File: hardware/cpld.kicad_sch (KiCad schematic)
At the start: 1 part, among them U26 ATF1508AS-10AU100

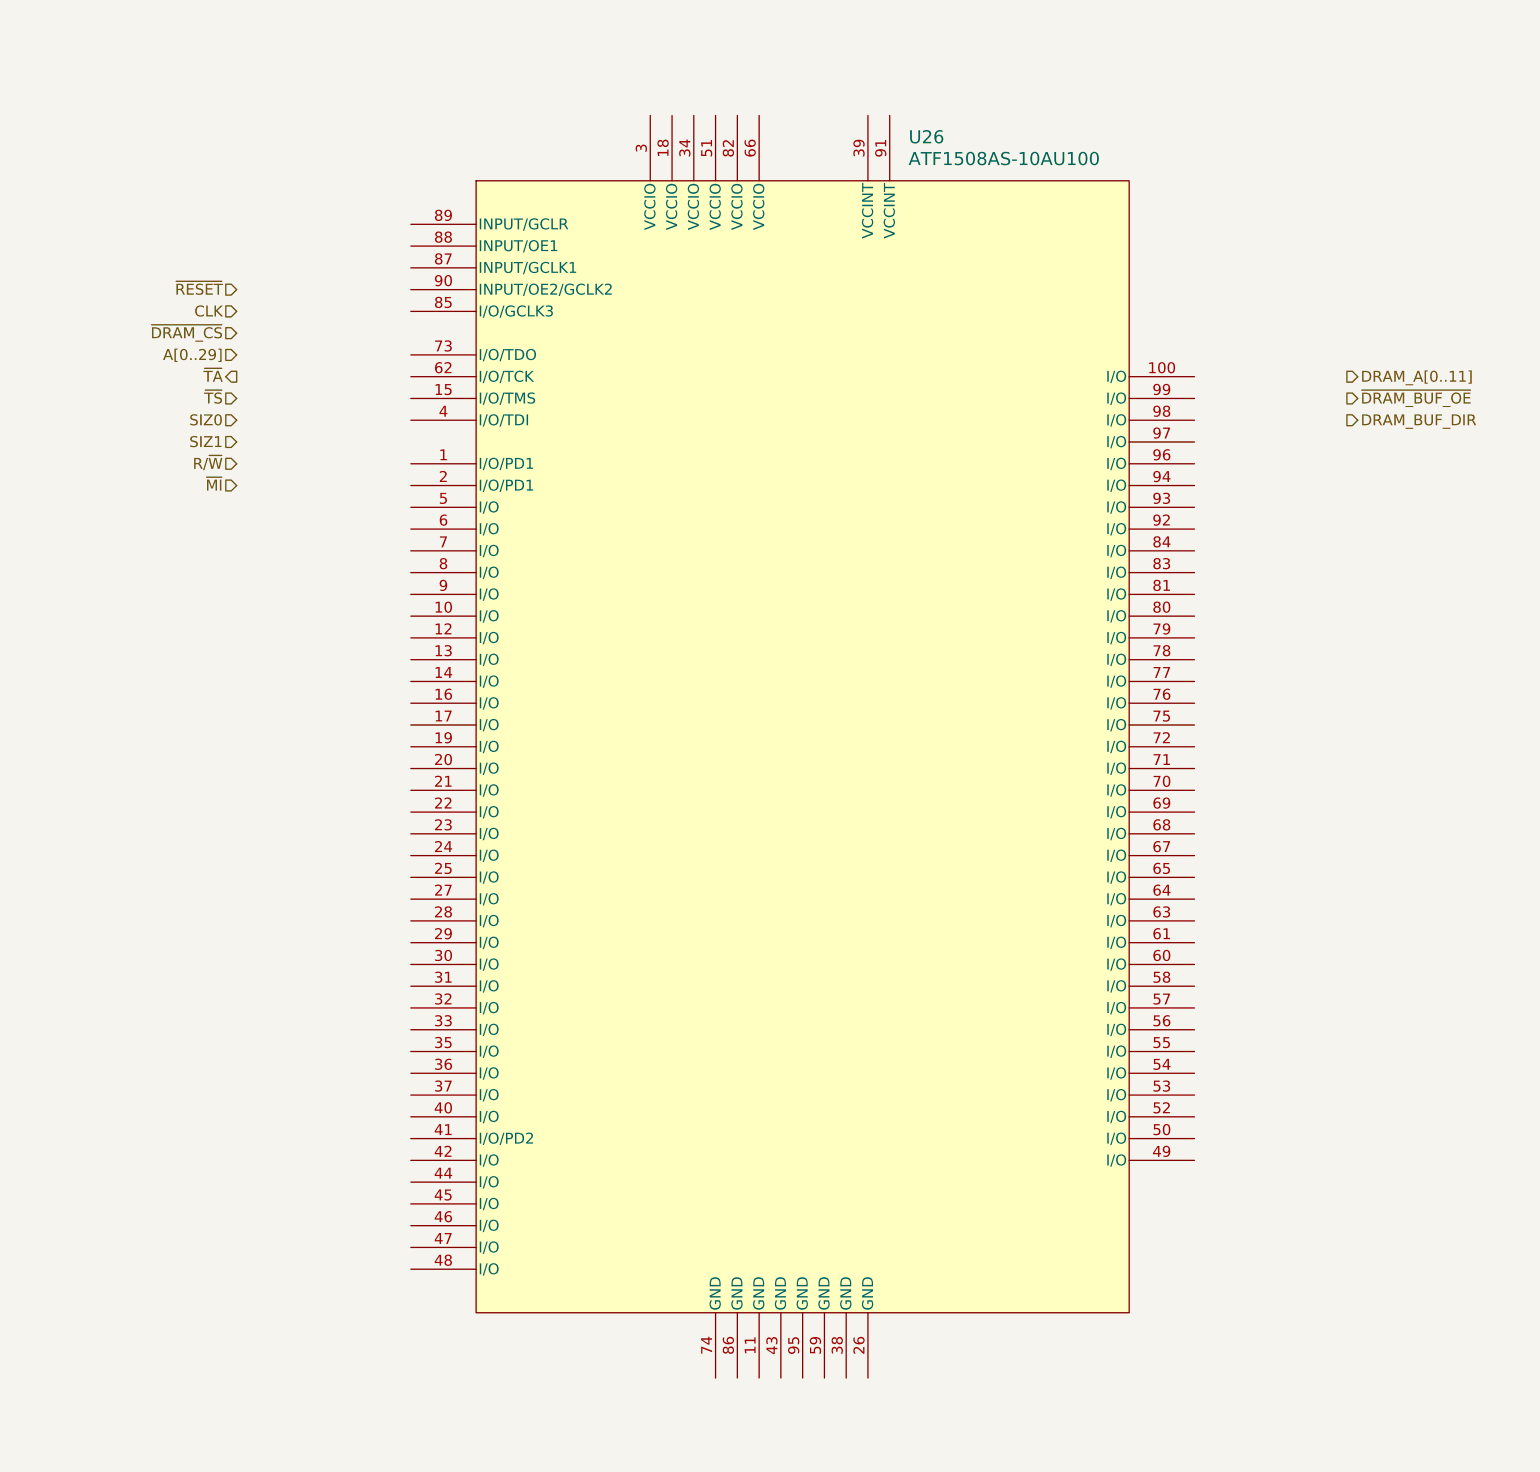
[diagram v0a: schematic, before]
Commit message: add interrupt logic, clean up modules
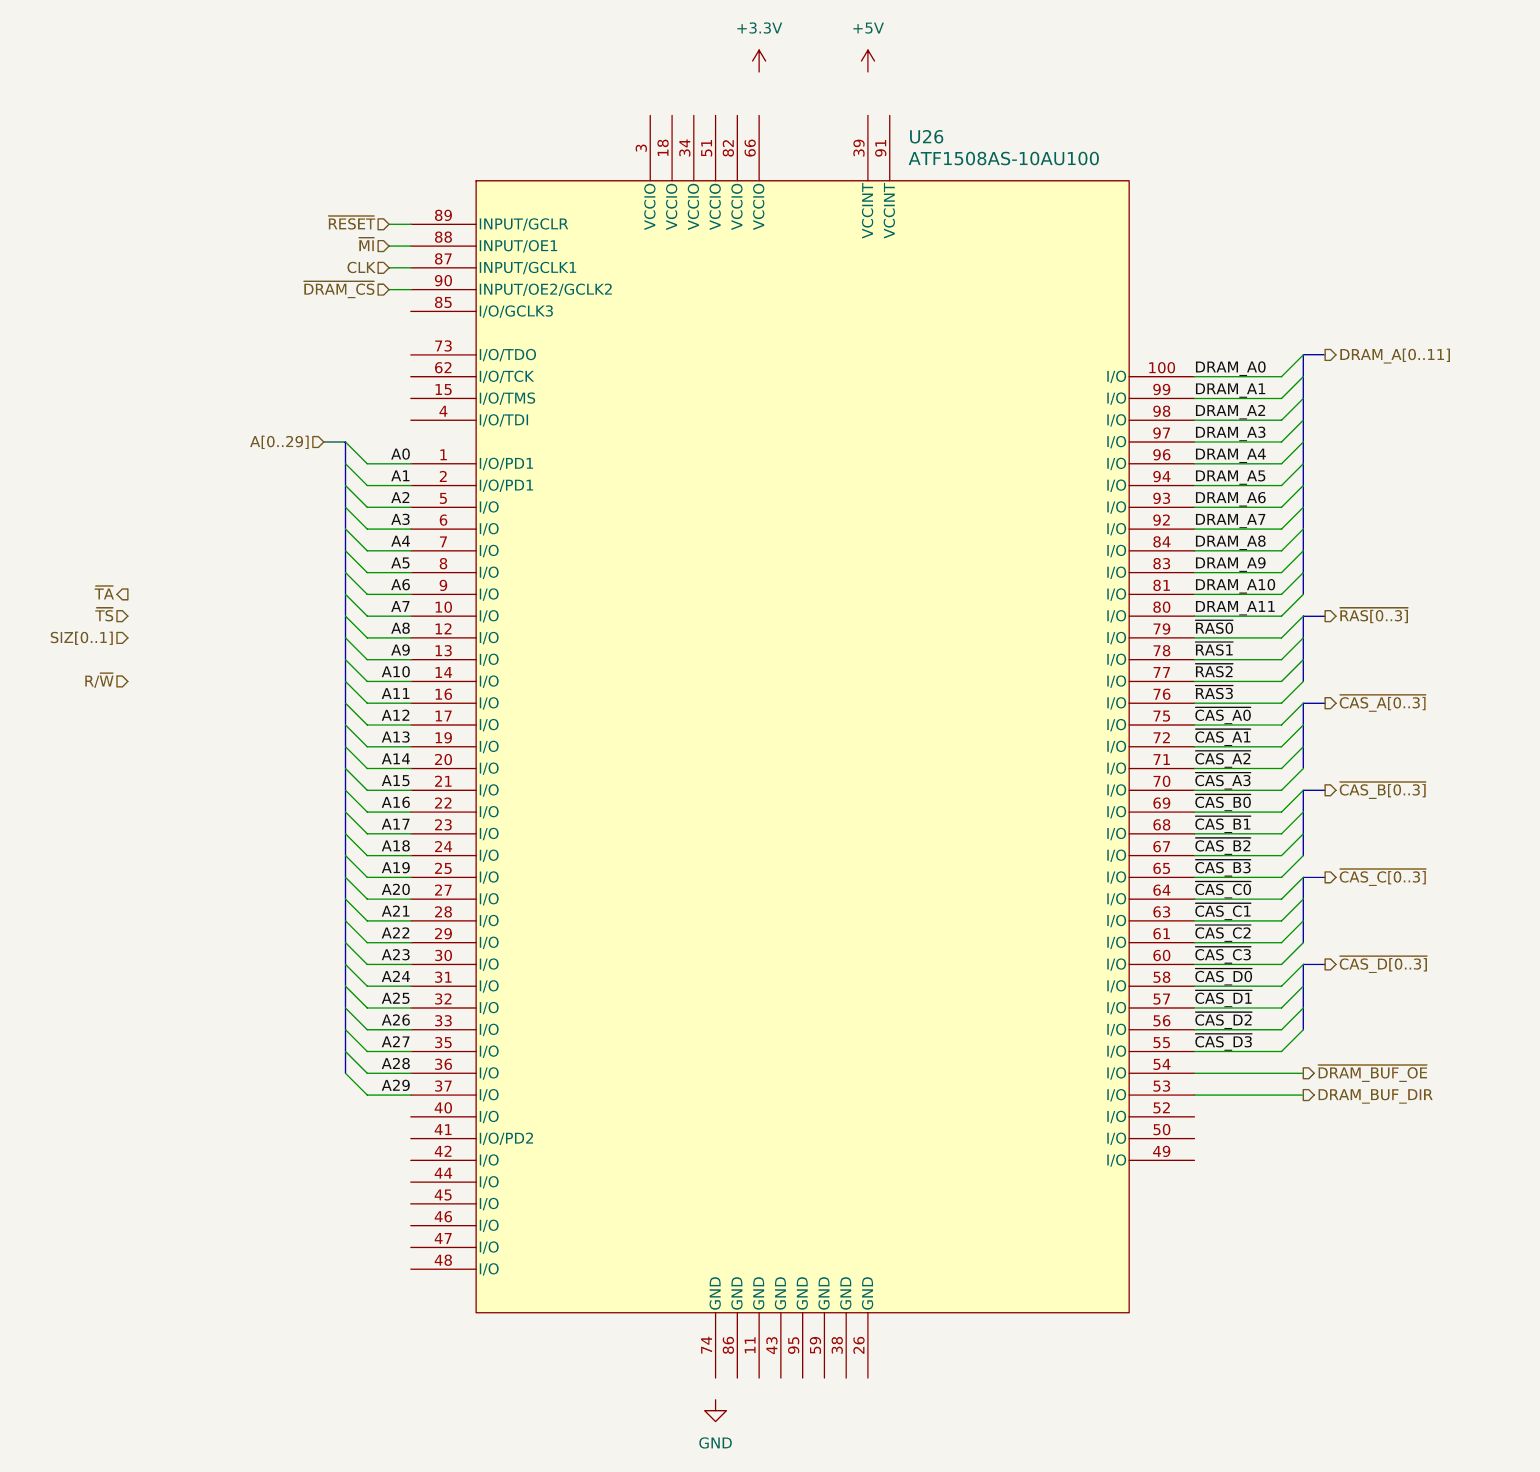
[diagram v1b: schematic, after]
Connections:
- net CLK: now also U26.87 (INPUT/GCLK1)
- net DRAM_BUF_DIR: now also U26.53 (I/O)
- net ~{DRAM_BUF_OE}: now also U26.54 (I/O)
- net ~{DRAM_CS}: now also U26.90 (INPUT/OE2/GCLK2)
- net ~{MI}: now also U26.88 (INPUT/OE1)
- net ~{RESET}: now also U26.89 (INPUT/GCLR)
- net A0: now reaches U26.1 (I/O/PD1)
- net A7: now reaches U26.10 (I/O)
- net DRAM_A0: now reaches U26.100 (I/O)
- net A8: now reaches U26.12 (I/O)
- net A9: now reaches U26.13 (I/O)
- net A10: now reaches U26.14 (I/O)
- net A11: now reaches U26.16 (I/O)
- net A12: now reaches U26.17 (I/O)
- net A13: now reaches U26.19 (I/O)
- net A1: now reaches U26.2 (I/O/PD1)
- net A14: now reaches U26.20 (I/O)
- net A15: now reaches U26.21 (I/O)
- net A16: now reaches U26.22 (I/O)
- net A17: now reaches U26.23 (I/O)
- net A18: now reaches U26.24 (I/O)
- net A19: now reaches U26.25 (I/O)
- net A20: now reaches U26.27 (I/O)
- net A21: now reaches U26.28 (I/O)
- net A22: now reaches U26.29 (I/O)
- net A23: now reaches U26.30 (I/O)
- net A24: now reaches U26.31 (I/O)
- net A25: now reaches U26.32 (I/O)
- net A26: now reaches U26.33 (I/O)
- net A27: now reaches U26.35 (I/O)
- net A28: now reaches U26.36 (I/O)
- net A29: now reaches U26.37 (I/O)
- net A2: now reaches U26.5 (I/O)
- net ~{CAS_D3}: now reaches U26.55 (I/O)
- net ~{CAS_D2}: now reaches U26.56 (I/O)
- net ~{CAS_D1}: now reaches U26.57 (I/O)
- net ~{CAS_D0}: now reaches U26.58 (I/O)
- net A3: now reaches U26.6 (I/O)
- net ~{CAS_C3}: now reaches U26.60 (I/O)
- net ~{CAS_C2}: now reaches U26.61 (I/O)
- net ~{CAS_C1}: now reaches U26.63 (I/O)
- net ~{CAS_C0}: now reaches U26.64 (I/O)
- net ~{CAS_B3}: now reaches U26.65 (I/O)
- net ~{CAS_B2}: now reaches U26.67 (I/O)
- net ~{CAS_B1}: now reaches U26.68 (I/O)
- net ~{CAS_B0}: now reaches U26.69 (I/O)
- net A4: now reaches U26.7 (I/O)
- net ~{CAS_A3}: now reaches U26.70 (I/O)
- net ~{CAS_A2}: now reaches U26.71 (I/O)
- net ~{CAS_A1}: now reaches U26.72 (I/O)
- net ~{CAS_A0}: now reaches U26.75 (I/O)
- net ~{RAS3}: now reaches U26.76 (I/O)
- net ~{RAS2}: now reaches U26.77 (I/O)
- net ~{RAS1}: now reaches U26.78 (I/O)
- net ~{RAS0}: now reaches U26.79 (I/O)
- net A5: now reaches U26.8 (I/O)
- net DRAM_A11: now reaches U26.80 (I/O)
- net DRAM_A10: now reaches U26.81 (I/O)
- net DRAM_A9: now reaches U26.83 (I/O)
- net DRAM_A8: now reaches U26.84 (I/O)
- net A6: now reaches U26.9 (I/O)
- net DRAM_A7: now reaches U26.92 (I/O)
- net DRAM_A6: now reaches U26.93 (I/O)
- net DRAM_A5: now reaches U26.94 (I/O)
- net DRAM_A4: now reaches U26.96 (I/O)
- net DRAM_A3: now reaches U26.97 (I/O)
- net DRAM_A2: now reaches U26.98 (I/O)
- net DRAM_A1: now reaches U26.99 (I/O)

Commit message: updates
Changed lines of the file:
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@@
     (effects (font (size 1.27 1.27)) (justify left))
   )
-  (hierarchical_label "A[0..29]" (shape input) (at 53.34 71.12 180) (fields_autoplaced)
+  (hierarchical_label "{ABUS}" (shape input) (at 53.34 71.12 180) (fields_autoplaced)
     (effects (font (size 1.27 1.27)) (justify right))
   )

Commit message: getting closer
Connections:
- net DRAM_BUF_DIR: no longer names the net of U26.53 (I/O)
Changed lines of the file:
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@@
-    (stroke (width 0) (type default))
-  )
-  (wire (pts (xy 154.94 147.32) (xy 167.64 147.32))
     (stroke (width 0) (type default))
   )
@@
   (hierarchical_label "~{MI}" (shape input) (at 60.96 48.26 180) (fields_autoplaced)
     (effects (font (size 1.27 1.27)) (justify right))
-  )
-  (hierarchical_label "DRAM_BUF_DIR" (shape output) (at 167.64 147.32 0) (fields_autoplaced)
-    (effects (font (size 1.27 1.27)) (justify left))
   )
   (hierarchical_label "~{CAS_D[0..3]}" (shape output) (at 170.18 132.08 0) (fields_autoplaced)
@@
     )
   )
-  (symbol (lib_id "power:+3.3V") (at 104.14 27.94 0) (unit 1)
+  (symbol (lib_id "power:+5V") (at 104.14 27.94 0) (unit 1)
     (in_bom yes) (on_board yes) (dnp no) (fields_autoplaced)
     (property "Reference" "#PWR0111" (at 104.14 31.75 0)
       (effects (font (size 1.27 1.27)) hide)
     )
-    (property "Value" "+3.3V" (at 104.14 22.86 0)
+    (property "Value" "+5V" (at 104.14 22.86 0)
       (effects (font (size 1.27 1.27)))
     )
